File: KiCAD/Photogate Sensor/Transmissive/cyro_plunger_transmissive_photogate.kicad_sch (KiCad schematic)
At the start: 48 parts, among them J1 FFC, J2 FFC Socket, J3 USB_B_Micro, J4 UPDI socket, J6 Conn_01x03_Socket, Q1 Q_NMOS_GSD, Q2 Q_NMOS_GSD, Q3 Q_NMOS_GSD, Q4 Q_NMOS_GSD, U1 5V LDO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

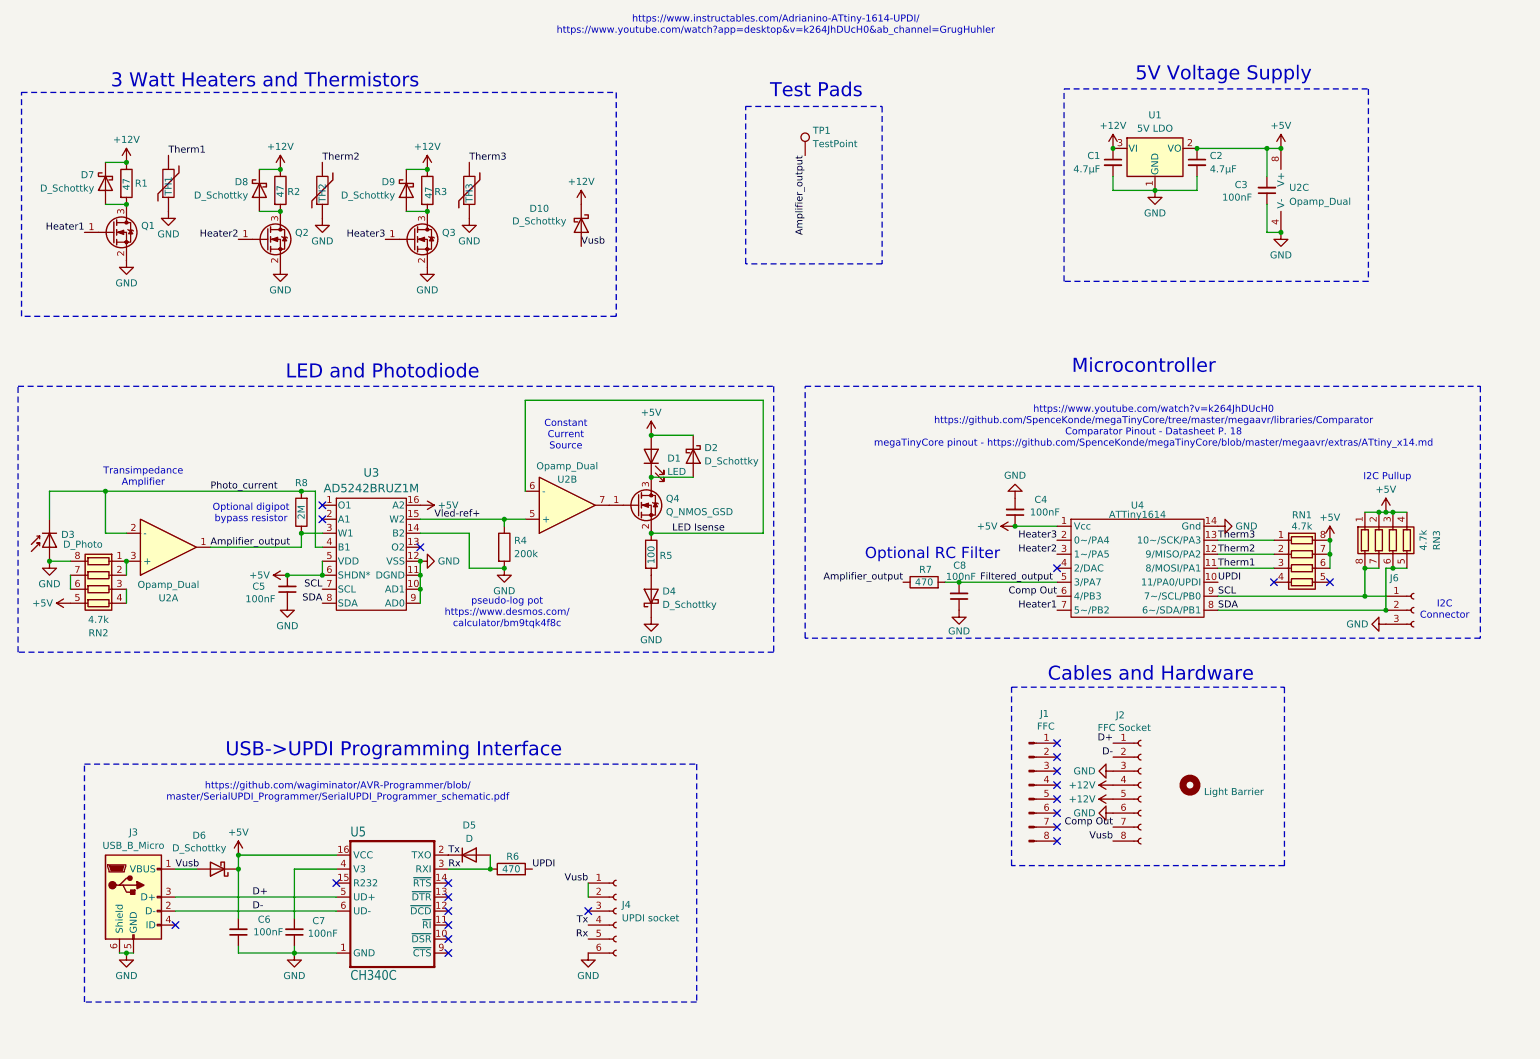
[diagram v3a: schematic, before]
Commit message: Panelize boards - improve 12V thermal pad
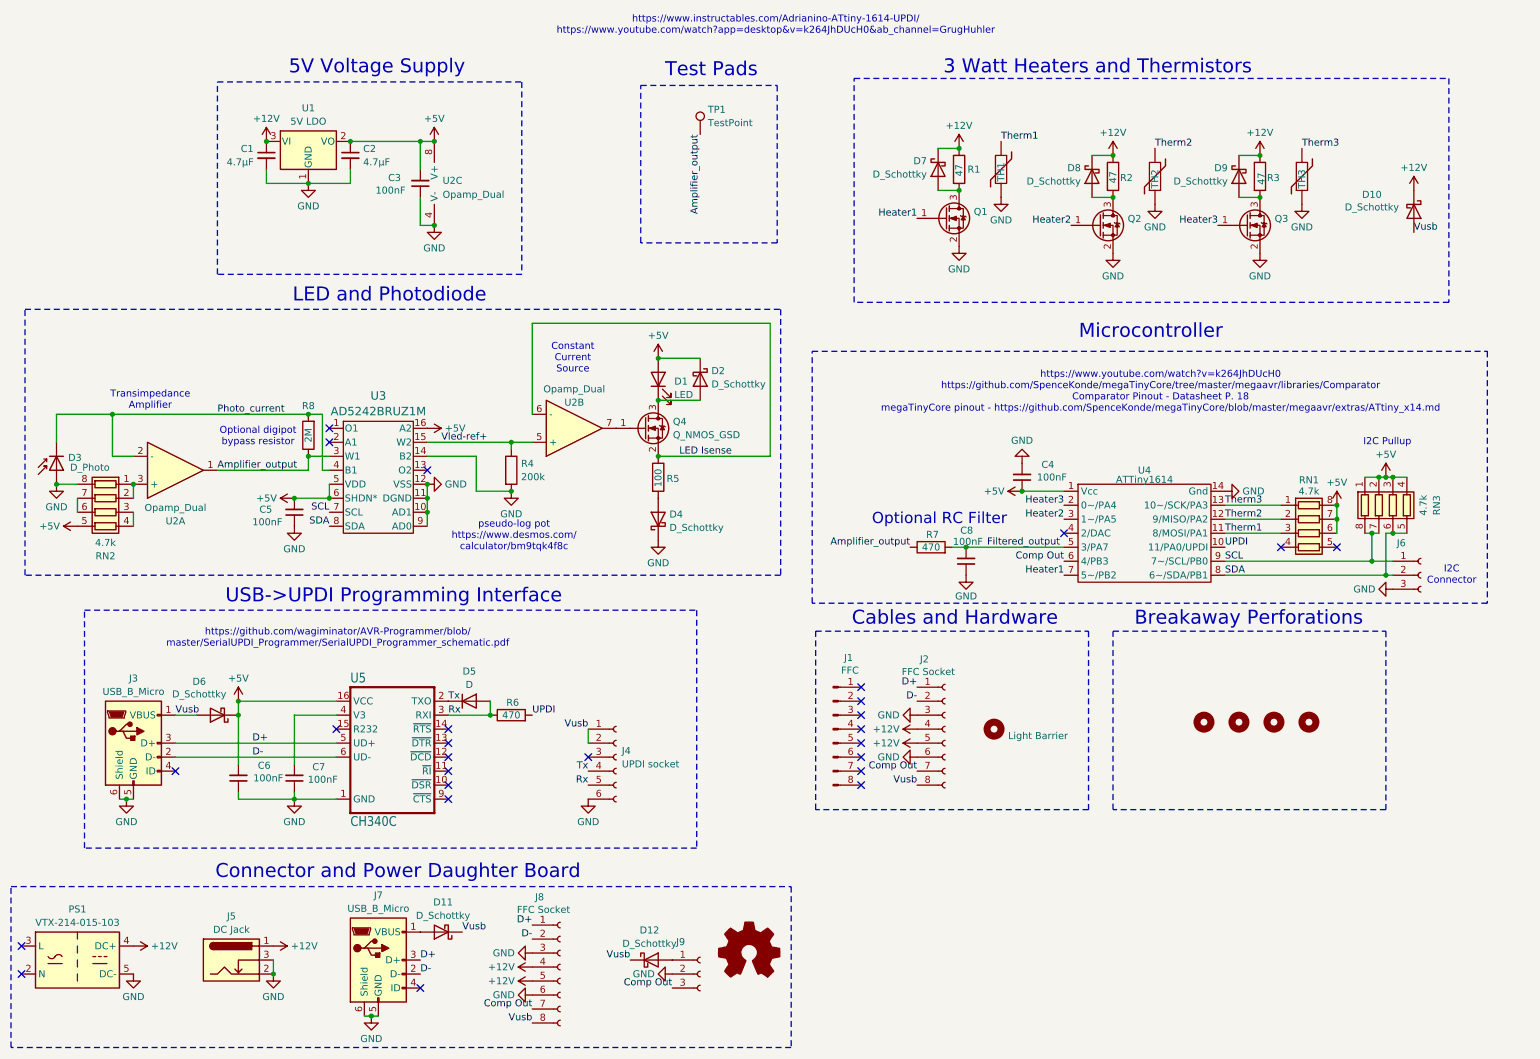
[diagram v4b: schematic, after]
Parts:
- added D11, D12: D_Schottky, Diode_SMD:D_SOD-323, symbol Device:D_Schottky
- added H2, H3, H4, H5: ~, Custom:mouse bite, symbol Mechanical:MountingHole
- added J5: DC Jack, Custom:TENSILITY_54-00165, symbol Connector:Barrel_Jack_Switch
- added J7: USB_B_Micro, Custom:CUI_UJ2-MIBH-G-SMT-TR, symbol Connector:USB_B_Micro
- added J8: FFC Socket, Custom:AMPHENOL_SFW8S-2STE1LF, symbol Connector:Conn_01x08_Socket
- added J9: Conn_01x03_Socket, Connector_PinSocket_2.54mm:PinSocket_1x03_P2.54mm_Vertical_SMD_Pin1Right, symbol Connector:Conn_01x03_Socket
- added PS1: VTX-214-015-103, symbol Converter_ACDC:VTX-214-015-103
- added SYM1: Logo_Open_Hardware_Small, Custom:polarity, symbol Graphic:Logo_Open_Hardware_Small
- J1: Manufacturer Parlex USA LLC -> Molex; Part 100R8-457B -> 0151670243
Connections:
- net +12V: now also J5.1, J8.4 (Pin_4), J8.5 (Pin_5), PS1.4 (DC+)
- net Comp Out: now also J8.7 (Pin_7), J9.3 (Pin_3)
- net D+: now also J7.3 (D+), J8.1 (Pin_1)
- net D-: now also J7.2 (D-), J8.2 (Pin_2)
- net GND: now also J5.2, J5.3, J7.5 (GND), J7.6 (Shield), J8.3 (Pin_3), J8.6 (Pin_6), J9.2 (Pin_2), PS1.5 (DC-)
- net Vusb: now also D11.1 (K), D12.1 (K), J8.8 (Pin_8)
- new net: D12.2 (A), J9.1 (Pin_1)
- new net: D11.2 (A), J7.1 (VBUS)
- no-connect marks 23 -> 26
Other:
- note added: "Breakaway Perforations"
- note added: "Connector and Power Daughter Board"
- moved on the sheet: C1, C2, C3, C4, C5, C6, C7, C8, D1, D10, D2, D3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

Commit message: replace silicon updi diode with schottky
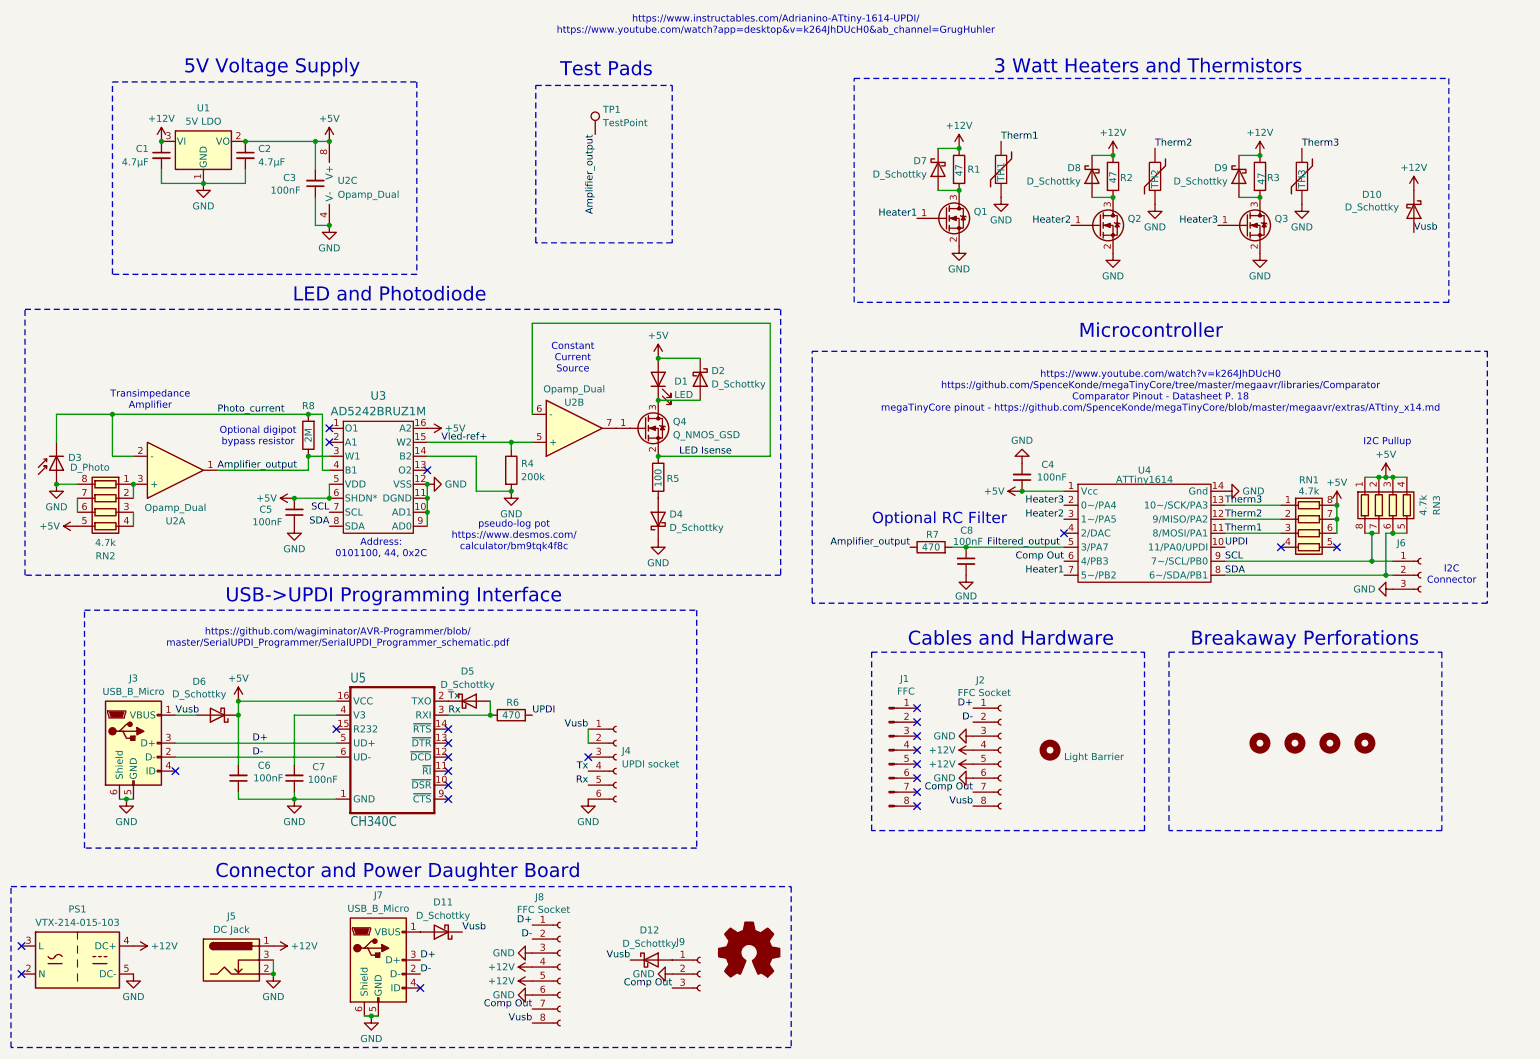
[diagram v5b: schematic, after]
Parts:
- removed D5: D, Diode_SMD:D_SOD-323, symbol Device:D
- added D5: D_Schottky, Diode_SMD:D_SOD-323, symbol Device:D_Schottky
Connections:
- net Rx: now also D5.2 (A)
- net Tx: now also D5.1 (K)
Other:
- note added: "Address: 0101100, 44, 0x2C"
- moved on the sheet: C1, C2, C3, J1, J2, TP1, U1, U2C

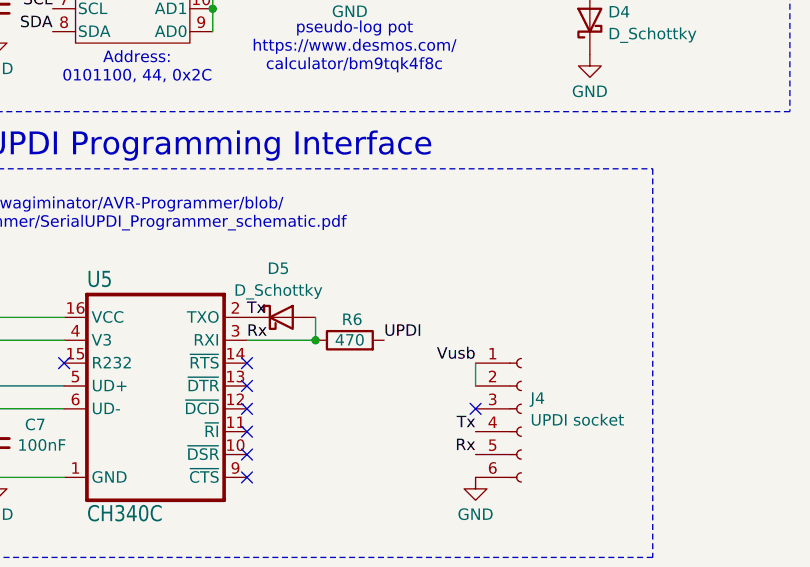
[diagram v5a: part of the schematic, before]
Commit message: heater control test with autotune PWM
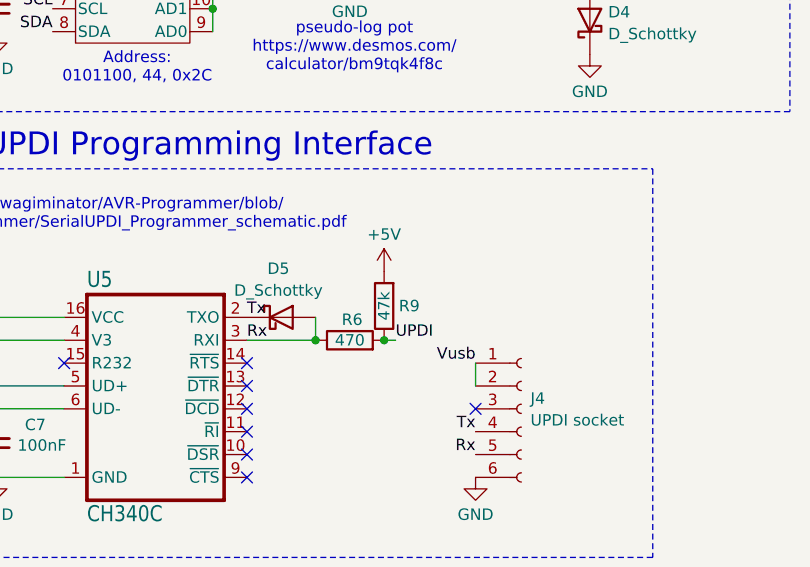
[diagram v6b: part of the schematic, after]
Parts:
- added R9: 47k, Resistor_SMD:R_0805_2012Metric, symbol Device:R
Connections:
- net +5V: now also R9.2
- net UPDI: now also R9.1
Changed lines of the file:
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@@
 	)
 	(junction
+		(at 109.22 132.08)
+		(diameter 0)
+		(color 0 0 0 0)
+	)
+	(junction
 		(at 66.04 147.32)
 		(diameter 0)
@@
 	(wire
 		(pts
+			(xy 109.22 132.08) (xy 110.49 132.08)
+		)
+		(stroke
+			(width 0)
+			(type default)
+		)
+	)
+	(wire
+		(pts
 			(xy 55.88 129.54) (xy 73.66 129.54)
 		)
@@
 	)
 	(label "UPDI"
-		(at 109.22 132.08 0)
+		(at 110.49 132.08 0)
 		(fields_autoplaced yes)
 		(effects
@@
 	)
 	(symbol
+		(lib_id "power:+5V")
+		(at 109.22 124.46 0)
+		(unit 1)
+		(exclude_from_sim no)
+		(in_bom yes)
+		(on_board yes)
+		(dnp no)
+		(fields_autoplaced yes)
+		(property "Reference" "#PWR049"
+			(at 109.22 128.27 0)
+			(effects
+				(font
+					(size 1.27 1.27)
+				)
+				(hide yes)
+			)
+		)
+		(property "Value" "+5V"
+			(at 109.22 120.3269 0)
+			(effects
+				(font
+					(size 1.27 1.27)
+				)
+			)
+		)
+		(property "Footprint" ""
+			(at 109.22 124.46 0)
+			(effects
+				(font
+					(size 1.27 1.27)
+				)
+				(hide yes)
+			)
+		)
+		(property "Datasheet" ""
+			(at 109.22 124.46 0)
+			(effects
+				(font
+					(size 1.27 1.27)
+				)
+				(hide yes)
+			)
+		)
+		(property "Description" "Power symbol creates a global label with name \"+5V\""
+			(at 109.22 124.46 0)
+			(effects
+				(font
+					(size 1.27 1.27)
+				)
+				(hide yes)
+			)
+		)
+		(pin "1"
+		)
+		(instances
+			(project "cyro_plunger_transmissive_photogate"
+				(path "/99ca36d5-bbf3-497e-815f-42a5447a2ddc"
+					(reference "#PWR049")
+					(unit 1)
+				)
+			)
+		)
+	)
+	(symbol
 		(lib_id "Device:R_Pack04")
 		(at 265.43 93.98 0)
@@
 					(unit 1)
 				)
+			)
+		)
+	)
+	(symbol
+		(lib_id "Device:R")
+		(at 109.22 128.27 180)
+		(unit 1)
+		(exclude_from_sim no)
+		(in_bom yes)
+		(on_board yes)
+		(dnp no)
+		(property "Reference" "R9"
+			(at 112.014 128.27 0)
+			(effects
+				(font
+					(size 1.27 1.27)
+				)
+			)
+		)
+		(property "Value" "47k"
+			(at 109.22 128.27 90)
+			(effects
+				(font
+					(size 1.27 1.27)
+				)
+			)
+		)
+		(property "Footprint" "Resistor_SMD:R_0805_2012Metric"
+			(at 110.998 128.27 90)
+			(effects
+				(font
+					(size 1.27 1.27)
+				)
+				(hide yes)
+			)
+		)
+		(property "Datasheet" "https://www.yageo.com/upload/media/product/app/datasheet/rchip/pyu-rp_51_rohs_l.pdf"
+			(at 109.22 128.27 0)
+			(effects
+				(font
+					(size 1.27 1.27)
+				)
+				(hide yes)
+			)
+		)
+		(property "Description" "470 Ohms ±1% 0.125W, 1/8W Chip Resistor 0805 (2012 Metric) Anti-Sulfur, Automotive AEC-Q200, Moisture Resistant Thin Film"
+			(at 109.22 128.27 0)
+			(effects
+				(font
+					(size 1.27 1.27)
+				)
+				(hide yes)
+			)
+		)
+		(property "Manufacturer" "YAGEO"
+			(at 109.22 128.27 0)
+			(effects
+				(font
+					(size 1.27 1.27)
+				)
+				(hide yes)
+			)
+		)
+		(property "Part" "RP0805FRE07470RL"
+			(at 109.22 128.27 0)
+			(effects
+				(font
+					(size 1.27 1.27)
+				)
+				(hide yes)
+			)
+		)
+		(pin "2"
+		)
+		(pin "1"
+		)
+		(instances
+			(project "cyro_plunger_transmissive_photogate"
+				(path "/99ca36d5-bbf3-497e-815f-42a5447a2ddc"
+					(reference "R9")
+					(unit 1)
+				)

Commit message: Better heater control, photodiode autocalibration
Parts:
- removed R9: 47k, Resistor_SMD:R_0805_2012Metric, symbol Device:R
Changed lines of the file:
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@@
 	)
 	(junction
-		(at 109.22 132.08)
-		(diameter 0)
-		(color 0 0 0 0)
-	)
-	(junction
 		(at 66.04 147.32)
 		(diameter 0)
@@
 	)
 	(symbol
-		(lib_id "power:+5V")
-		(at 109.22 124.46 0)
-		(unit 1)
-		(exclude_from_sim no)
-		(in_bom yes)
-		(on_board yes)
-		(dnp no)
-		(fields_autoplaced yes)
-		(property "Reference" "#PWR049"
-			(at 109.22 128.27 0)
-			(effects
-				(font
-					(size 1.27 1.27)
-				)
-				(hide yes)
-			)
-		)
-		(property "Value" "+5V"
-			(at 109.22 120.3269 0)
-			(effects
-				(font
-					(size 1.27 1.27)
-				)
-			)
-		)
-		(property "Footprint" ""
-			(at 109.22 124.46 0)
-			(effects
-				(font
-					(size 1.27 1.27)
-				)
-				(hide yes)
-			)
-		)
-		(property "Datasheet" ""
-			(at 109.22 124.46 0)
-			(effects
-				(font
-					(size 1.27 1.27)
-				)
-				(hide yes)
-			)
-		)
-		(property "Description" "Power symbol creates a global label with name \"+5V\""
-			(at 109.22 124.46 0)
-			(effects
-				(font
-					(size 1.27 1.27)
-				)
-				(hide yes)
-			)
-		)
-		(pin "1"
-		)
-		(instances
-			(project "cyro_plunger_transmissive_photogate"
-				(path "/99ca36d5-bbf3-497e-815f-42a5447a2ddc"
-					(reference "#PWR049")
-					(unit 1)
-				)
-			)
-		)
-	)
-	(symbol
 		(lib_id "Device:R_Pack04")
 		(at 265.43 93.98 0)
@@
 					(unit 1)
 				)
-			)
-		)
-	)
-	(symbol
-		(lib_id "Device:R")
-		(at 109.22 128.27 180)
-		(unit 1)
-		(exclude_from_sim no)
-		(in_bom yes)
-		(on_board yes)
-		(dnp no)
-		(property "Reference" "R9"
-			(at 112.014 128.27 0)
-			(effects
-				(font
-					(size 1.27 1.27)
-				)
-			)
-		)
-		(property "Value" "47k"
-			(at 109.22 128.27 90)
-			(effects
-				(font
-					(size 1.27 1.27)
-				)
-			)
-		)
-		(property "Footprint" "Resistor_SMD:R_0805_2012Metric"
-			(at 110.998 128.27 90)
-			(effects
-				(font
-					(size 1.27 1.27)
-				)
-				(hide yes)
-			)
-		)
-		(property "Datasheet" "https://www.yageo.com/upload/media/product/app/datasheet/rchip/pyu-rp_51_rohs_l.pdf"
-			(at 109.22 128.27 0)
-			(effects
-				(font
-					(size 1.27 1.27)
-				)
-				(hide yes)
-			)
-		)
-		(property "Description" "470 Ohms ±1% 0.125W, 1/8W Chip Resistor 0805 (2012 Metric) Anti-Sulfur, Automotive AEC-Q200, Moisture Resistant Thin Film"
-			(at 109.22 128.27 0)
-			(effects
-				(font
-					(size 1.27 1.27)
-				)
-				(hide yes)
-			)
-		)
-		(property "Manufacturer" "YAGEO"
-			(at 109.22 128.27 0)
-			(effects
-				(font
-					(size 1.27 1.27)
-				)
-				(hide yes)
-			)
-		)
-		(property "Part" "RP0805FRE07470RL"
-			(at 109.22 128.27 0)
-			(effects
-				(font
-					(size 1.27 1.27)
-				)
-				(hide yes)
-			)
-		)
-		(pin "2"
-		)
-		(pin "1"
-		)
-		(instances
-			(project "cyro_plunger_transmissive_photogate"
-				(path "/99ca36d5-bbf3-497e-815f-42a5447a2ddc"
-					(reference "R9")
-					(unit 1)
-				)
